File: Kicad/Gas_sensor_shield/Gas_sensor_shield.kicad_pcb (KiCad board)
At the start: 2 copper layers, 68.6 x 53.3 mm, 25 parts, among them P1 Power, P2 Analog, P3 Digital, P4 Digital, P5 CONN_01X01, P6 CONN_01X01, P7 CONN_01X01, P8 CONN_01X01, U1 LTC1050, U2 Gas_Sensor, U3 RN2483_Breakout

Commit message: modified the circuit board and routed
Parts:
- removed the R7 at (142.7, 99.1)
- removed R8: 330, Resistor_THT:R_Axial_DIN0204_L3.6mm_D1.6mm_P7.62mm_Horizontal
- added RV1: R_POT, Potentiometer_THT:Potentiometer_ACP_CA9-V10_Vertical, F.Cu at (142.7, 108.6)
- renumbered R9 to R7
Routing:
- net Net-(C2-Pad1): track 0.00 -> 67.3 mm
- net Net-(C1-Pad1): track 0.00 -> 65.1 mm
- net /A1: track 0.00 -> 63.3 mm
- net /A0: track 0.00 -> 59.2 mm
- net /D10: track 0.00 -> 55.5 mm
- net /D11: track 0.00 -> 46.5 mm
- net +3V3: track 0.00 -> 43.3 mm
- net /D12: track 0.00 -> 37.2 mm
- net /D6(**): track 0.00 -> 33.2 mm
- net Net-(C2-Pad2): track 0.00 -> 31.4 mm
- net +5V: track 0.00 -> 25.6 mm
- net /Gas_sensor: track 0.00 -> 11.0 mm
- net /D8: track 0.00 -> 9.84 mm
- net Net-(D1-Pad2): track 0.00 -> 8.04 mm

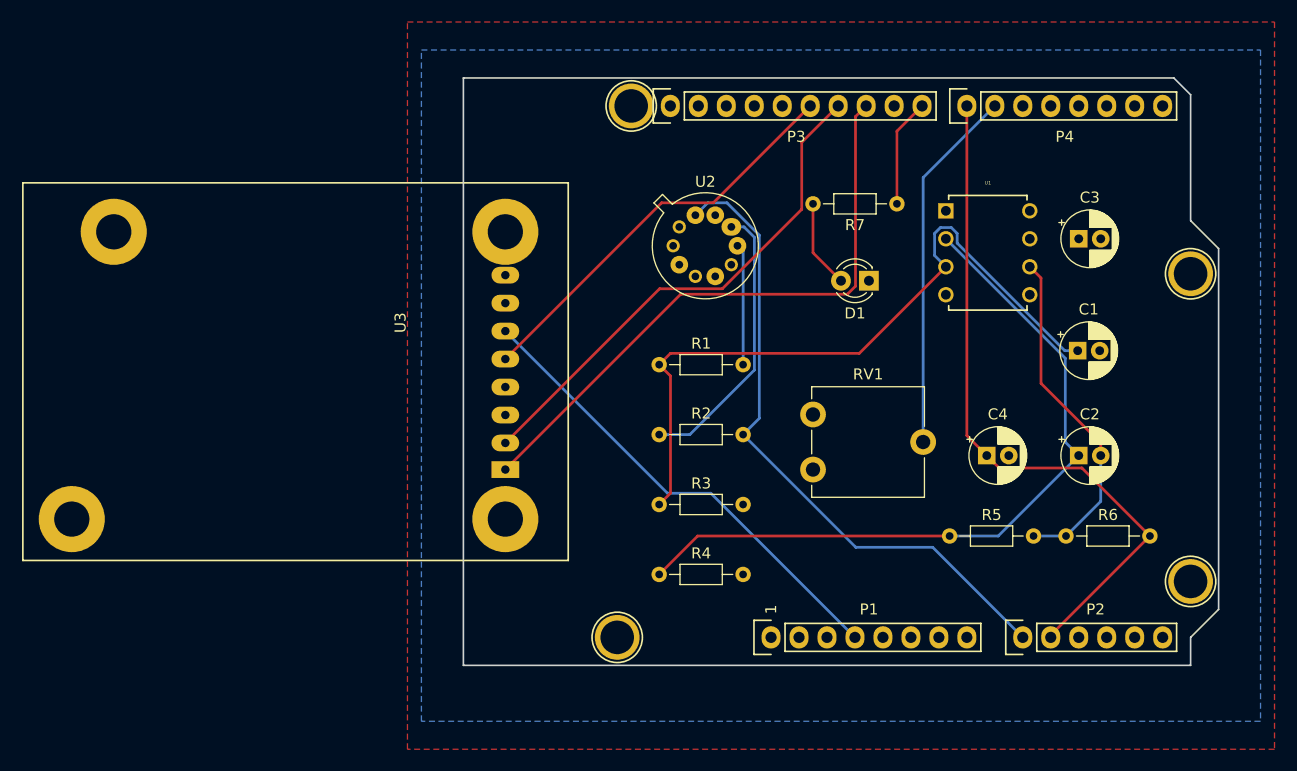
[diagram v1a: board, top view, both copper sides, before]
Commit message: added images of kicad
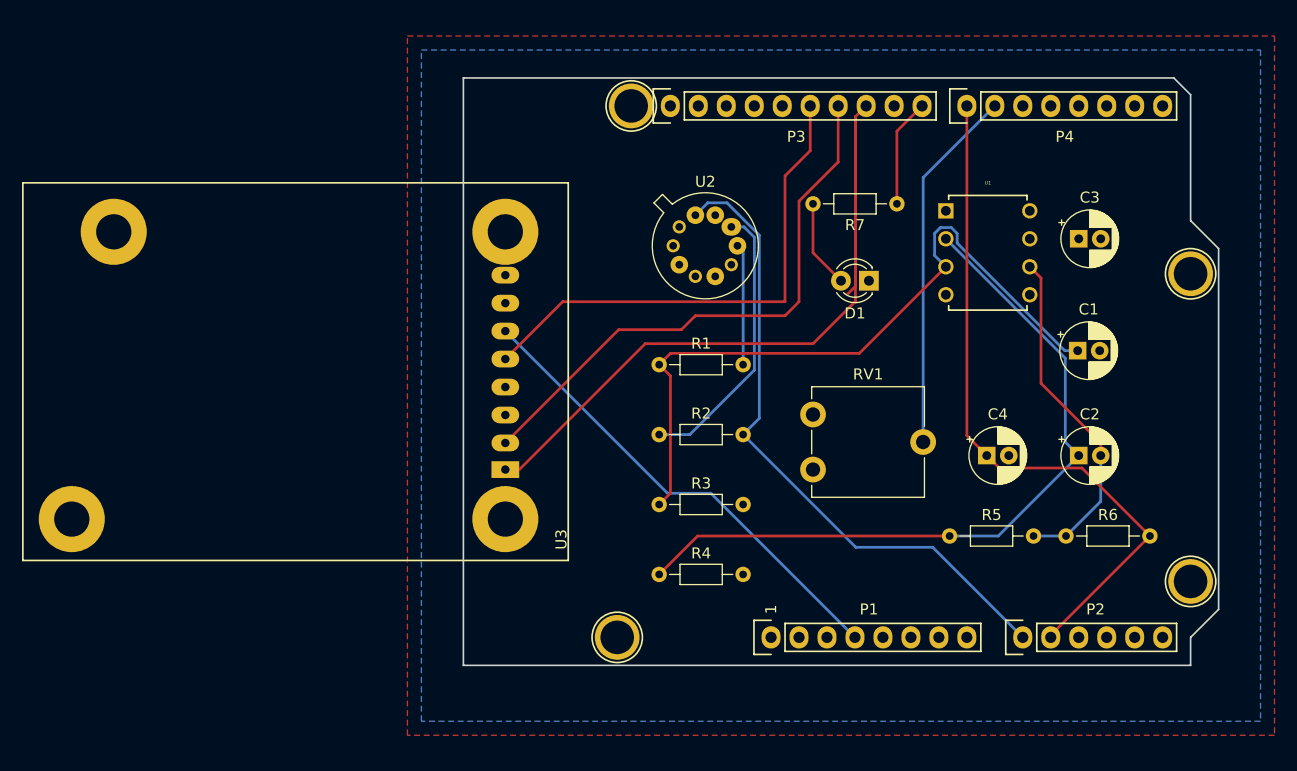
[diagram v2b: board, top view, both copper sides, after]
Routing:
- net /D10: track 55.5 -> 72.7 mm
- net /D12: track 37.2 -> 46.3 mm
- net /D11: track 46.5 -> 51.2 mm
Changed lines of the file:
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@@
     (thickness 1.6)
     (drawings 27)
-    (tracks 72)
+    (tracks 80)
     (zones 0)
     (modules 24)
@@
   (module My_Package:RN2483_breakout (layer F.Cu)
     (at 114.808 108.585 90)
-    (fp_text reference U3 (at 13.335 -9.525 90) (layer F.SilkS)
+    (fp_text reference U3 (at -6.35 5.08 90) (layer F.SilkS)
       (effects (font (size 1 1) (thickness 0.15)))
     )
@@
   (segment (start 142.748 88.9) (end 145.288 91.44) (width 0.25) (layer F.Cu) (net 21))
   (segment (start 142.748 84.455) (end 142.748 88.9) (width 0.25) (layer F.Cu) (net 21))
-  (segment (start 133.696086 84.362914) (end 142.494 75.565) (width 0.25) (layer F.Cu) (net 26))
-  (segment (start 128.997086 84.362914) (end 133.696086 84.362914) (width 0.25) (layer F.Cu) (net 26))
-  (segment (start 114.808 98.552) (end 128.997086 84.362914) (width 0.25) (layer F.Cu) (net 26))
-  (segment (start 141.722999 78.876001) (end 145.034 75.565) (width 0.25) (layer F.Cu) (net 27))
-  (segment (start 141.722999 84.957666) (end 141.722999 78.876001) (width 0.25) (layer F.Cu) (net 27))
-  (segment (start 134.513579 92.167086) (end 141.722999 84.957666) (width 0.25) (layer F.Cu) (net 27))
-  (segment (start 128.812914 92.167086) (end 134.513579 92.167086) (width 0.25) (layer F.Cu) (net 27))
-  (segment (start 114.808 106.172) (end 128.812914 92.167086) (width 0.25) (layer F.Cu) (net 27))
-  (segment (start 146.602999 76.536001) (end 147.574 75.565) (width 0.25) (layer F.Cu) (net 28))
+  (segment (start 140.208 81.915) (end 142.494 79.629) (width 0.25) (layer F.Cu) (net 26))
+  (segment (start 140.208 93.345) (end 140.208 81.915) (width 0.25) (layer F.Cu) (net 26))
+  (segment (start 120.015 93.345) (end 140.208 93.345) (width 0.25) (layer F.Cu) (net 26))
+  (segment (start 142.494 79.629) (end 142.494 75.565) (width 0.25) (layer F.Cu) (net 26))
+  (segment (start 114.808 98.552) (end 120.015 93.345) (width 0.25) (layer F.Cu) (net 26))
+  (segment (start 114.808 106.172) (end 125.095 95.885) (width 0.25) (layer F.Cu) (net 27))
+  (segment (start 130.795665 95.885) (end 132.065665 94.615) (width 0.25) (layer F.Cu) (net 27))
+  (segment (start 125.095 95.885) (end 130.795665 95.885) (width 0.25) (layer F.Cu) (net 27))
+  (segment (start 132.065665 94.615) (end 140.208 94.615) (width 0.25) (layer F.Cu) (net 27))
+  (segment (start 145.034 80.651998) (end 145.034 75.565) (width 0.25) (layer F.Cu) (net 27))
+  (segment (start 145.034 80.651998) (end 141.478 84.207998) (width 0.25) (layer F.Cu) (net 27))
+  (segment (start 141.478 84.207998) (end 141.478 93.345) (width 0.25) (layer F.Cu) (net 27))
+  (segment (start 141.478 93.345) (end 140.208 94.615) (width 0.25) (layer F.Cu) (net 27))
   (segment (start 146.602999 91.938003) (end 146.602999 76.536001) (width 0.25) (layer F.Cu) (net 28))
   (segment (start 145.876001 92.665001) (end 146.602999 91.938003) (width 0.25) (layer F.Cu) (net 28))
-  (segment (start 130.727999 92.665001) (end 145.876001 92.665001) (width 0.25) (layer F.Cu) (net 28))
-  (segment (start 114.808 108.585) (end 130.727999 92.665001) (width 0.25) (layer F.Cu) (net 28))
+  (segment (start 114.808 108.585) (end 116.078 108.585) (width 0.25) (layer F.Cu) (net 28))
+  (segment (start 116.078 108.585) (end 127.508 97.155) (width 0.25) (layer F.Cu) (net 28))
+  (segment (start 146.602999 76.536001) (end 147.574 75.565) (width 0.25) (layer F.Cu) (net 28))
+  (segment (start 142.748 97.155) (end 146.602999 93.300001) (width 0.25) (layer F.Cu) (net 28))
+  (segment (start 146.602999 93.300001) (end 146.602999 76.536001) (width 0.25) (layer F.Cu) (net 28))
+  (segment (start 127.508 97.155) (end 142.748 97.155) (width 0.25) (layer F.Cu) (net 28))
   (segment (start 150.368 77.851) (end 152.654 75.565) (width 0.25) (layer F.Cu) (net 30))
   (segment (start 150.368 84.455) (end 150.368 77.851) (width 0.25) (layer F.Cu) (net 30))
@@
   (segment (start 136.398 88.775) (end 135.888 88.265) (width 0.25) (layer B.Cu) (net 38))
   (segment (start 136.398 99.06) (end 136.398 88.775) (width 0.25) (layer B.Cu) (net 38))
-  (zone (net 2) (net_name +5V) (layer F.Cu) (hatch edge 0.508)
-    (connect_pads (clearance 0.508))
-    (min_thickness 0.254)
-    (fill yes (arc_segments 32) (thermal_gap 0.508) (thermal_bridge_width 0.508))
-    (polygon
-      (pts
-        (xy 184.658 133.985) (xy 105.918 133.985) (xy 105.918 67.945) (xy 184.658 67.945)
-      )
-    )
-  )
   (zone (net 3) (net_name GND) (layer B.Cu) (hatch edge 0.508)
     (connect_pads (clearance 0.508))
@@
       )
     )
+  )
+  (zone (net 2) (net_name +5V) (layer F.Cu) (hatch edge 0.508)
+    (connect_pads (clearance 0.508))
+    (min_thickness 0.254)
+    (fill yes (arc_segments 32) (thermal_gap 0.508) (thermal_bridge_width 0.508))
+    (polygon
+      (pts
+        (xy 184.658 132.715) (xy 105.918 132.715) (xy 105.918 69.215) (xy 184.658 69.215)
+      )
+    )
